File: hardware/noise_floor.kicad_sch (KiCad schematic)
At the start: 10 parts, among them J1 Input, J2 Output, J3 DC Power, J4 Edge/Effect Connector 1 (Edge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, J5 Edge/Effect Connector 2 (Edge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, J6 Edge/Node Connector 1 (Edge S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, J7 Edge/Node Connector 2 (Edge S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, J8 Edge/Node Connector 1 (Node S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, J9 Edge/Node Connector 2 (Node S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, SW1 Footswitch

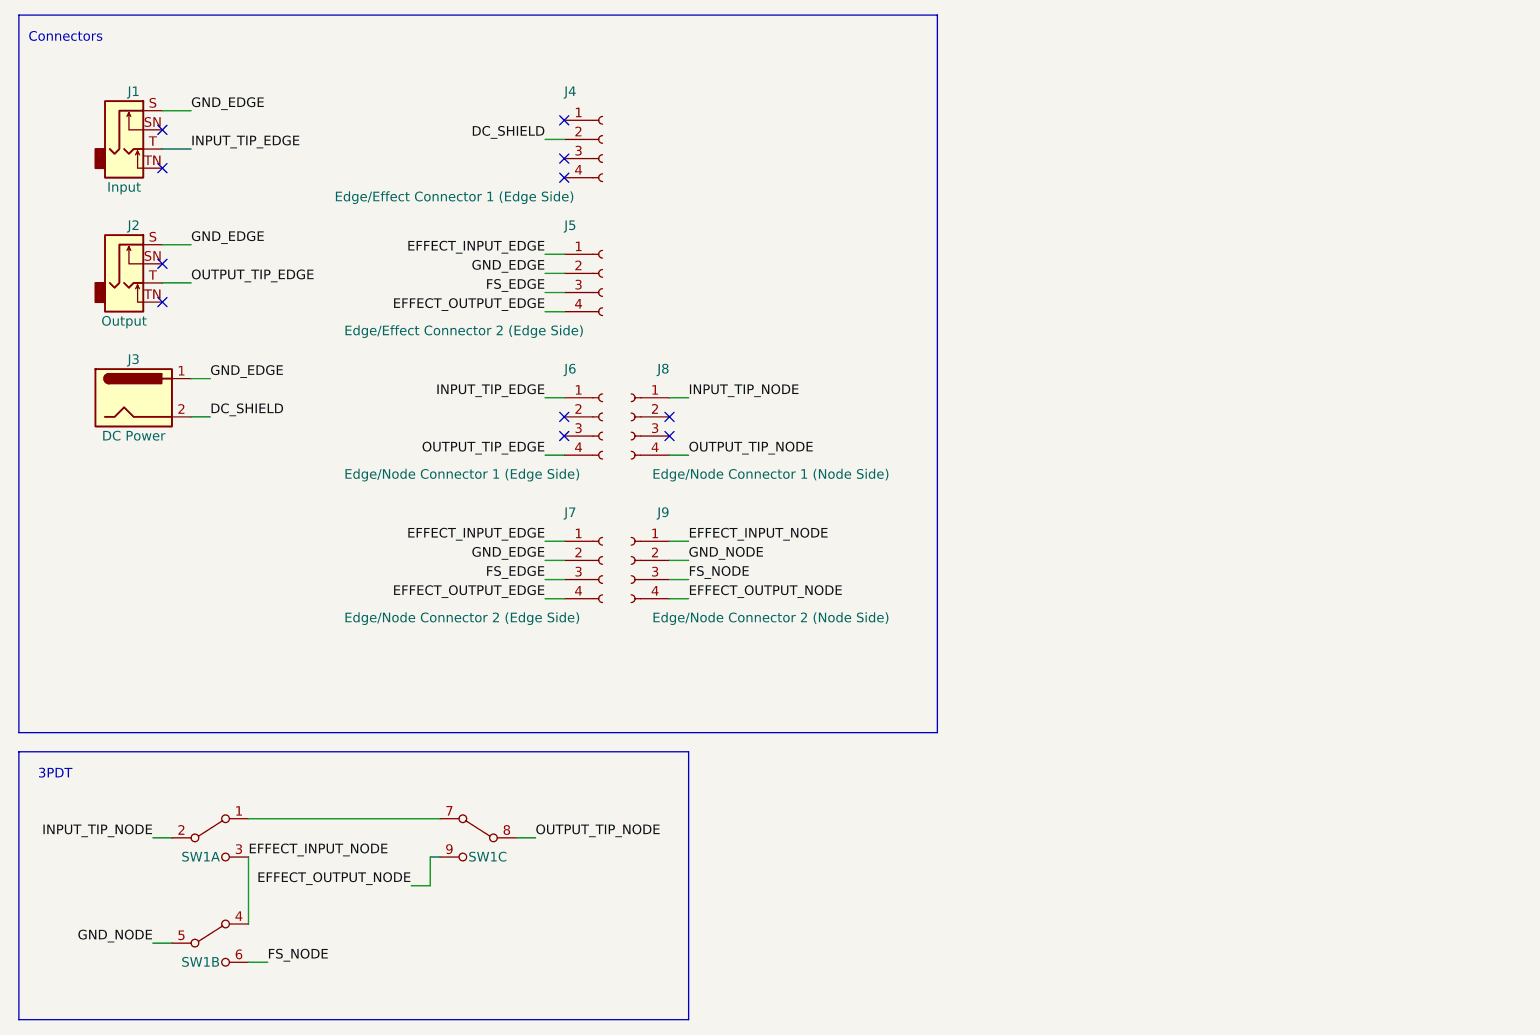
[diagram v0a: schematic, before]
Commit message: change name to Noise Floor
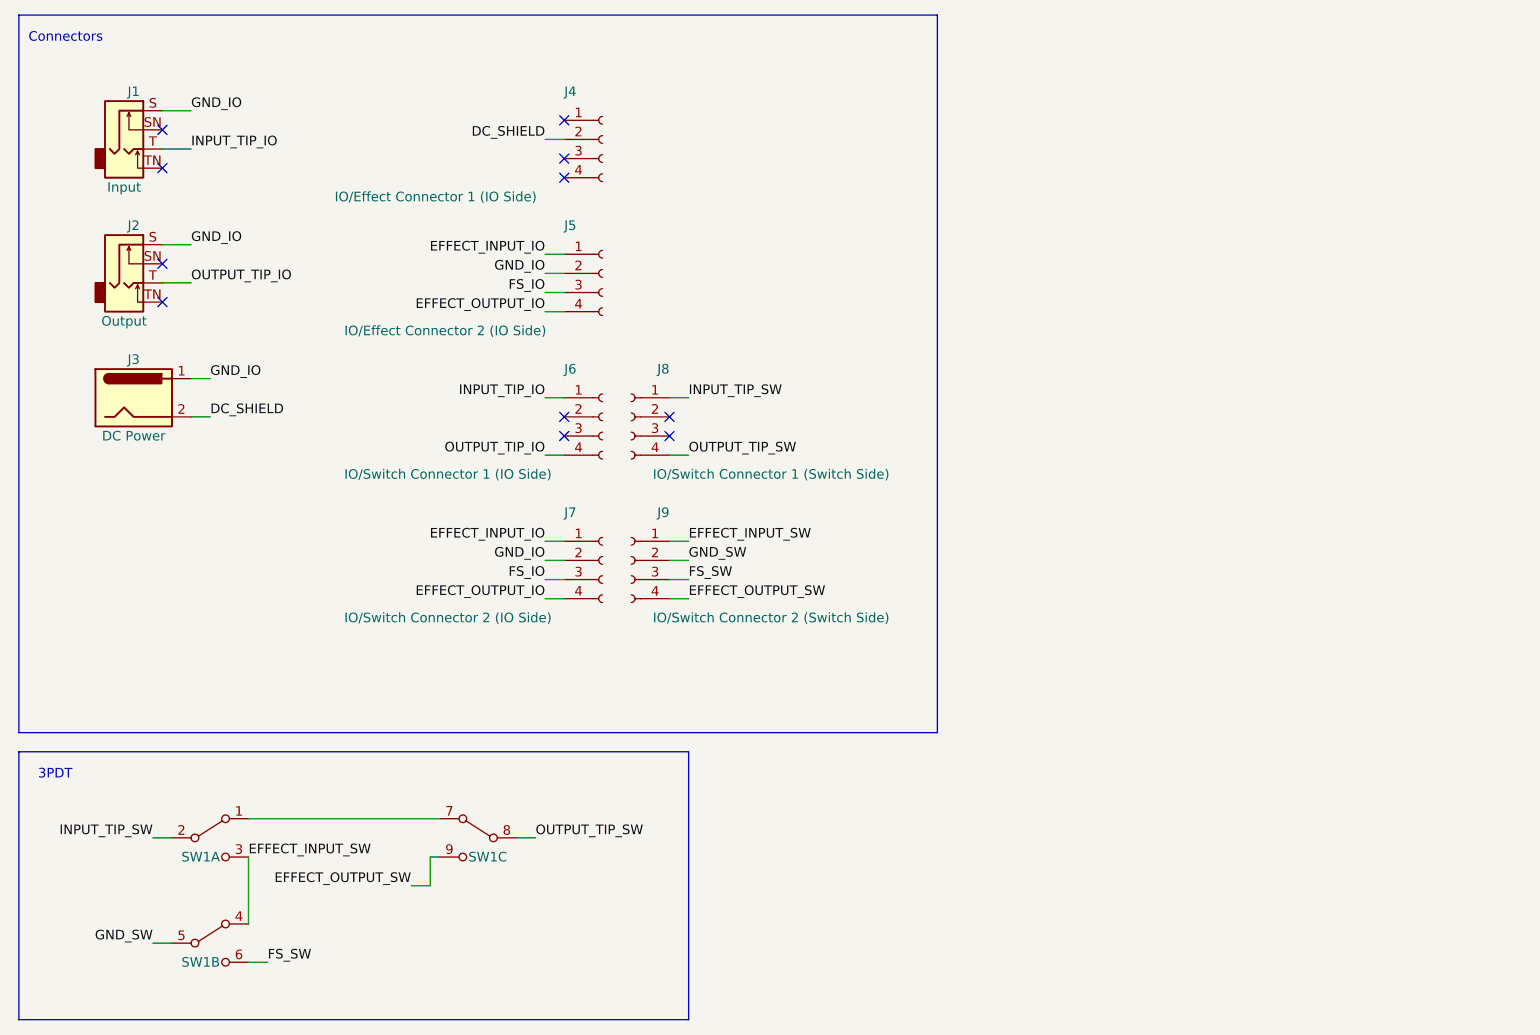
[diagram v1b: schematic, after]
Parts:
- J4: value Edge/Effect Connector 1 (Edge Side) -> IO/Effect Connector 1 (IO Side)
- J5: value Edge/Effect Connector 2 (Edge Side) -> IO/Effect Connector 2 (IO Side)
- J6: value Edge/Node Connector 1 (Edge Side) -> IO/Switch Connector 1 (IO Side)
- J7: value Edge/Node Connector 2 (Edge Side) -> IO/Switch Connector 2 (IO Side)
- J8: value Edge/Node Connector 1 (Node Side) -> IO/Switch Connector 1 (Switch Side)
- J9: value Edge/Node Connector 2 (Node Side) -> IO/Switch Connector 2 (Switch Side)
- SW1: footprint attack_graph:SW_3PDT_SOLDER_LUGS -> noise_floor:SW_3PDT_SOLDER_LUGS; symbol attack_graph:SW_STOMP_3PDT -> noise_floor:SW_STOMP_3PDT
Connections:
- net EFFECT_INPUT_EDGE renamed EFFECT_INPUT_IO
- net EFFECT_INPUT_NODE renamed EFFECT_INPUT_SW
- net EFFECT_OUTPUT_EDGE renamed EFFECT_OUTPUT_IO
- net EFFECT_OUTPUT_NODE renamed EFFECT_OUTPUT_SW
- net FS_EDGE renamed FS_IO
- net FS_NODE renamed FS_SW
- net GND_EDGE renamed GND_IO
- net GND_NODE renamed GND_SW
- net INPUT_TIP_EDGE renamed INPUT_TIP_IO
- net INPUT_TIP_NODE renamed INPUT_TIP_SW
- net OUTPUT_TIP_EDGE renamed OUTPUT_TIP_IO
- net OUTPUT_TIP_NODE renamed OUTPUT_TIP_SW
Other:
- title: Attack Graph interface board -> Noise Floor Interface Boards

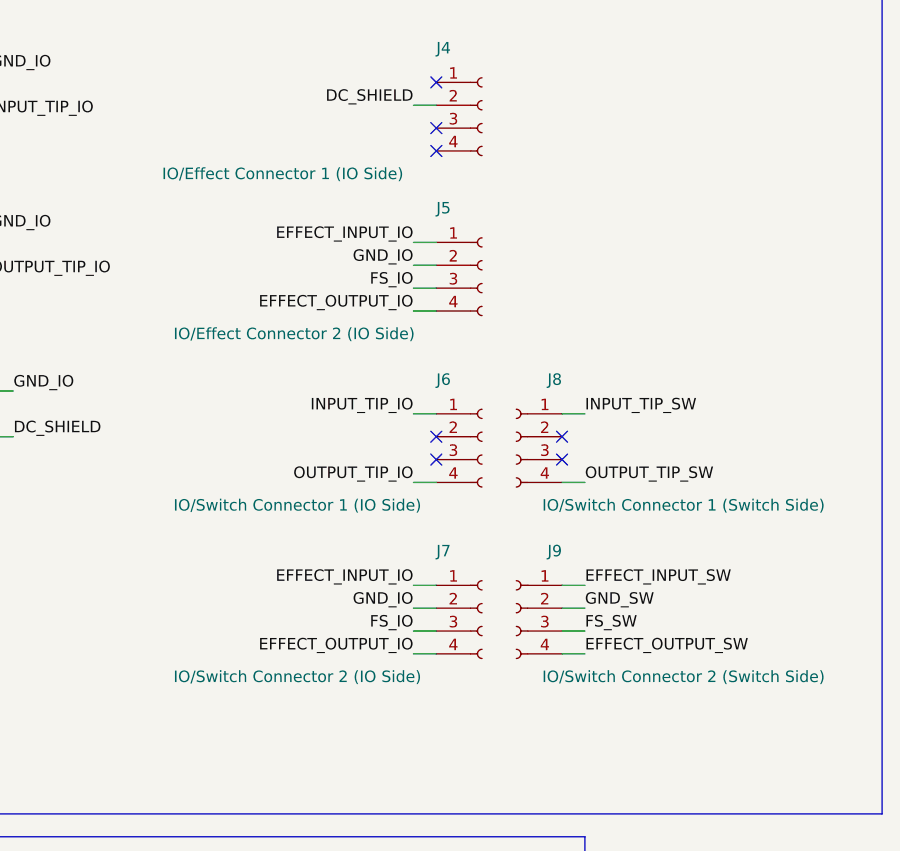
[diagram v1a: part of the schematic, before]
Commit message: fix ordering of IO/Switch board connectors
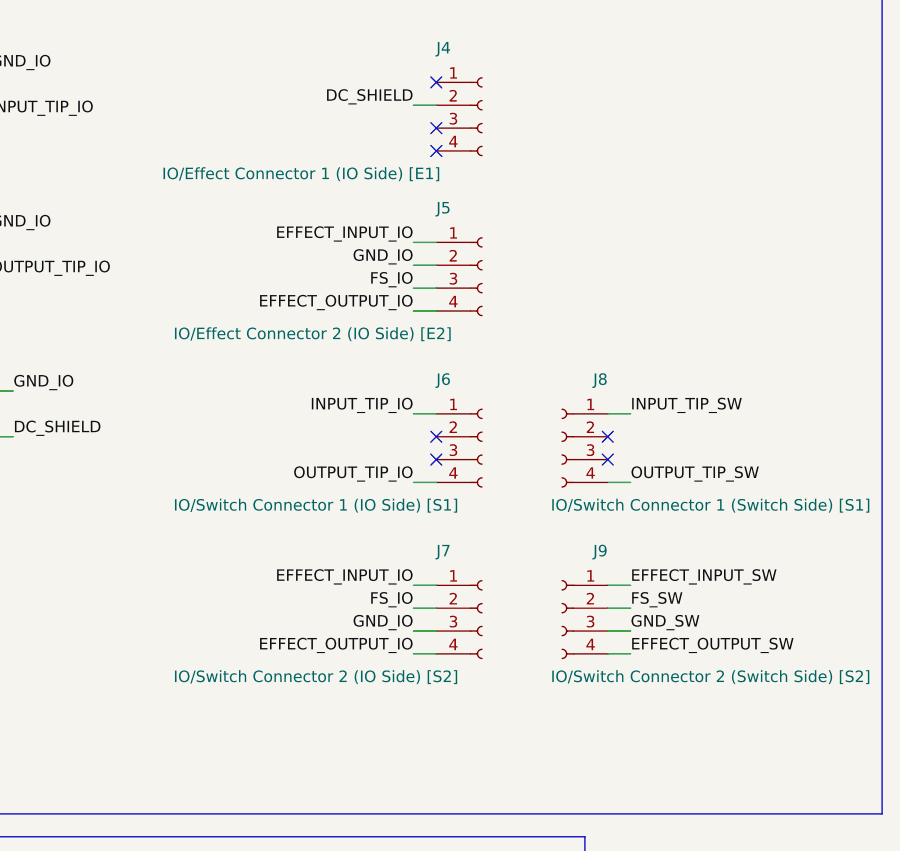
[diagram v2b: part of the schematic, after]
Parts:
- J4: value IO/Effect Connector 1 (IO Side) -> IO/Effect Connector 1 (IO Side) [E1]
- J5: value IO/Effect Connector 2 (IO Side) -> IO/Effect Connector 2 (IO Side) [E2]
- J6: value IO/Switch Connector 1 (IO Side) -> IO/Switch Connector 1 (IO Side) [S1]
- J7: value IO/Switch Connector 2 (IO Side) -> IO/Switch Connector 2 (IO Side) [S2]
- J8: value IO/Switch Connector 1 (Switch Side) -> IO/Switch Connector 1 (Switch Side) [S1]
- J9: value IO/Switch Connector 2 (Switch Side) -> IO/Switch Connector 2 (Switch Side) [S2]
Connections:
- net FS_IO: now also J7.2 (Pin_2); no longer J7.3 (Pin_3)
- net FS_SW: now also J9.2 (Pin_2); no longer J9.3 (Pin_3)
- net GND_IO: now also J7.3 (Pin_3); no longer J7.2 (Pin_2)
- net GND_SW: now also J9.3 (Pin_3); no longer J9.2 (Pin_2)
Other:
- moved on the sheet: J8, J9
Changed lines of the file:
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@@
   (no_connect (at 86.36 69.85))
   (no_connect (at 86.36 35.56))
-  (no_connect (at 100.33 67.31))
+  (no_connect (at 105.41 67.31))
   (no_connect (at 33.02 52.07))
   (no_connect (at 33.02 29.21))
@@
   (no_connect (at 86.36 27.94))
   (no_connect (at 86.36 33.02))
-  (no_connect (at 100.33 69.85))
-  (wire (pts (xy 102.87 72.39) (xy 100.33 72.39))
+  (no_connect (at 105.41 69.85))
+  (wire (pts (xy 107.95 72.39) (xy 105.41 72.39))
     (stroke (width 0) (type default))
   )
@@
     (stroke (width 0) (type default))
   )
-  (wire (pts (xy 102.87 91.44) (xy 100.33 91.44))
+  (wire (pts (xy 107.95 91.44) (xy 105.41 91.44))
     (stroke (width 0) (type default))
   )
@@
     (stroke (width 0) (type default))
   )
-  (wire (pts (xy 102.87 83.82) (xy 100.33 83.82))
-    (stroke (width 0) (type default))
-  )
-  (wire (pts (xy 102.87 86.36) (xy 100.33 86.36))
-    (stroke (width 0) (type default))
-  )
-  (wire (pts (xy 102.87 64.77) (xy 100.33 64.77))
+  (wire (pts (xy 107.95 83.82) (xy 105.41 83.82))
+    (stroke (width 0) (type default))
+  )
+  (wire (pts (xy 107.95 86.36) (xy 105.41 86.36))
+    (stroke (width 0) (type default))
+  )
+  (wire (pts (xy 107.95 64.77) (xy 105.41 64.77))
     (stroke (width 0) (type default))
   )
@@
     (stroke (width 0) (type default))
   )
-  (wire (pts (xy 102.87 88.9) (xy 100.33 88.9))
+  (wire (pts (xy 107.95 88.9) (xy 105.41 88.9))
     (stroke (width 0) (type default))
   )
@@
     (effects (font (size 1.27 1.27)) (justify right bottom))
   )
-  (label "INPUT_TIP_SW" (at 102.87 64.77 0)
+  (label "INPUT_TIP_SW" (at 107.95 64.77 0) (fields_autoplaced)
     (effects (font (size 1.27 1.27)) (justify left bottom))
   )
@@
     (effects (font (size 1.27 1.27)) (justify left bottom))
   )
-  (label "FS_SW" (at 102.87 88.9 0) (fields_autoplaced)
-    (effects (font (size 1.27 1.27)) (justify left bottom))
-  )
-  (label "EFFECT_INPUT_SW" (at 102.87 83.82 0)
+  (label "GND_SW" (at 107.95 88.9 0) (fields_autoplaced)
+    (effects (font (size 1.27 1.27)) (justify left bottom))
+  )
+  (label "EFFECT_INPUT_SW" (at 107.95 83.82 0) (fields_autoplaced)
     (effects (font (size 1.27 1.27)) (justify left bottom))
   )
@@
     )
   )
-  (label "GND_SW" (at 102.87 86.36 0) (fields_autoplaced)
+  (label "FS_SW" (at 107.95 86.36 0) (fields_autoplaced)
     (effects (font (size 1.27 1.27)) (justify left bottom))
   )
@@
     (effects (font (size 1.27 1.27)) (justify left bottom))
   )
-  (label "EFFECT_OUTPUT_SW" (at 102.87 91.44 0)
+  (label "EFFECT_OUTPUT_SW" (at 107.95 91.44 0) (fields_autoplaced)
     (effects (font (size 1.27 1.27)) (justify left bottom))
   )
@@
     (effects (font (size 1.27 1.27)) (justify right bottom))
   )
-  (label "FS_IO" (at 83.82 88.9 180) (fields_autoplaced)
+  (label "GND_IO" (at 83.82 88.9 180) (fields_autoplaced)
     (effects (font (size 1.27 1.27)) (justify right bottom))
   )
@@
     (effects (font (size 1.27 1.27)) (justify left bottom))
   )
-  (label "GND_IO" (at 83.82 86.36 180) (fields_autoplaced)
+  (label "FS_IO" (at 83.82 86.36 180) (fields_autoplaced)
     (effects (font (size 1.27 1.27)) (justify right bottom))
   )
@@
     )
   )
-  (label "OUTPUT_TIP_SW" (at 102.87 72.39 0) (fields_autoplaced)
+  (label "OUTPUT_TIP_SW" (at 107.95 72.39 0) (fields_autoplaced)
     (effects (font (size 1.27 1.27)) (justify left bottom))
   )
@@
       (effects (font (size 1.27 1.27)) (justify left))
     )
-    (property "Value" "IO/Switch Connector 1 (IO Side)" (at 57.15 74.93 0)
+    (property "Value" "IO/Switch Connector 1 (IO Side) [S1]" (at 57.15 74.93 0)
       (effects (font (size 1.27 1.27)) (justify left))
     )
@@
       (effects (font (size 1.27 1.27)) (justify left))
     )
-    (property "Value" "IO/Switch Connector 2 (IO Side)" (at 57.15 93.98 0)
+    (property "Value" "IO/Switch Connector 2 (IO Side) [S2]" (at 57.15 93.98 0)
       (effects (font (size 1.27 1.27)) (justify left))
     )
@@
       (effects (font (size 1.27 1.27)) (justify left))
     )
-    (property "Value" "IO/Effect Connector 2 (IO Side)" (at 57.15 55.88 0)
+    (property "Value" "IO/Effect Connector 2 (IO Side) [E2]" (at 57.15 55.88 0)
       (effects (font (size 1.27 1.27)) (justify left))
     )
@@
     )
   )
-  (symbol (lib_id "Connector:Conn_01x04_Socket") (at 95.25 86.36 0) (mirror y) (unit 1)
-    (in_bom yes) (on_board yes) (dnp no)
-    (property "Reference" "J9" (at 100.33 80.01 0)
-      (effects (font (size 1.27 1.27)) (justify left))
-    )
-    (property "Value" "IO/Switch Connector 2 (Switch Side)" (at 129.54 93.98 0)
-      (effects (font (size 1.27 1.27)) (justify left))
-    )
-    (property "Footprint" "Connector_Molex:Molex_PicoBlade_53047-0410_1x04_P1.25mm_Vertical" (at 95.25 86.36 0)
-      (effects (font (size 1.27 1.27)) hide)
-    )
-    (property "Datasheet" "~" (at 95.25 86.36 0)
+  (symbol (lib_id "Connector:Conn_01x04_Socket") (at 100.33 86.36 0) (mirror y) (unit 1)
+    (in_bom yes) (on_board yes) (dnp no)
+    (property "Reference" "J9" (at 105.41 80.01 0)
+      (effects (font (size 1.27 1.27)) (justify left))
+    )
+    (property "Value" "IO/Switch Connector 2 (Switch Side) [S2]" (at 134.62 93.98 0)
+      (effects (font (size 1.27 1.27)) (justify left))
+    )
+    (property "Footprint" "Connector_Molex:Molex_PicoBlade_53047-0410_1x04_P1.25mm_Vertical" (at 100.33 86.36 0)
+      (effects (font (size 1.27 1.27)) hide)
+    )
+    (property "Datasheet" "~" (at 100.33 86.36 0)
       (effects (font (size 1.27 1.27)) hide)
     )
@@
     )
   )
-  (symbol (lib_id "Connector:Conn_01x04_Socket") (at 95.25 67.31 0) (mirror y) (unit 1)
-    (in_bom yes) (on_board yes) (dnp no)
-    (property "Reference" "J8" (at 100.33 60.96 0)
-      (effects (font (size 1.27 1.27)) (justify left))
-    )
-    (property "Value" "IO/Switch Connector 1 (Switch Side)" (at 129.54 74.93 0)
-      (effects (font (size 1.27 1.27)) (justify left))
-    )
-    (property "Footprint" "Connector_Molex:Molex_PicoBlade_53047-0410_1x04_P1.25mm_Vertical" (at 95.25 67.31 0)
-      (effects (font (size 1.27 1.27)) hide)
-    )
-    (property "Datasheet" "~" (at 95.25 67.31 0)
+  (symbol (lib_id "Connector:Conn_01x04_Socket") (at 100.33 67.31 0) (mirror y) (unit 1)
+    (in_bom yes) (on_board yes) (dnp no)
+    (property "Reference" "J8" (at 105.41 60.96 0)
+      (effects (font (size 1.27 1.27)) (justify left))
+    )
+    (property "Value" "IO/Switch Connector 1 (Switch Side) [S1]" (at 134.62 74.93 0)
+      (effects (font (size 1.27 1.27)) (justify left))
+    )
+    (property "Footprint" "Connector_Molex:Molex_PicoBlade_53047-0410_1x04_P1.25mm_Vertical" (at 100.33 67.31 0)
+      (effects (font (size 1.27 1.27)) hide)
+    )
+    (property "Datasheet" "~" (at 100.33 67.31 0)
       (effects (font (size 1.27 1.27)) hide)
     )
@@
       (effects (font (size 1.27 1.27)) (justify left))
     )
-    (property "Value" "IO/Effect Connector 1 (IO Side)" (at 55.88 38.1 0)
-      (effects (font (size 1.27 1.27)) (justify left))
-    )
+    (property "Value" "IO/Effect Connector 1 (IO Side)  [E1]" (at 55.88 38.1 0)
+      (effects (font (size 1.27 1.27)) (justify left))
+    )
